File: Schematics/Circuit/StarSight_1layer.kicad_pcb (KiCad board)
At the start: 2 copper layers, 40 parts, among them IC1 LM2956-5V, J1 IR1, J10 Line1, J11 Conn_01x02, J12 Conn_01x02, J13 Conn_01x02, J14 ultSound1, J15 Conn_02x02_Counter_Clockwise, J16 ultSound1, J17 Conn_02x02_Counter_Clockwise, J18 ultSound1, J19 Conn_02x02_Counter_Clockwise, J2 Line5, J20 ultSound1, J21 Conn_01x01, J22 Conn_01x01, J23 Conn_01x01, J3 IR1, J4 Line4, J5 IR1, J6 Line3, J7 IR1, J8 Line2, J9 IR1, K1 RELAY, K2 RELAY, P1 CONN_13X2, P2 Power, Q1 Q_NMOS_GDS, Q2 Q_NMOS_GDS

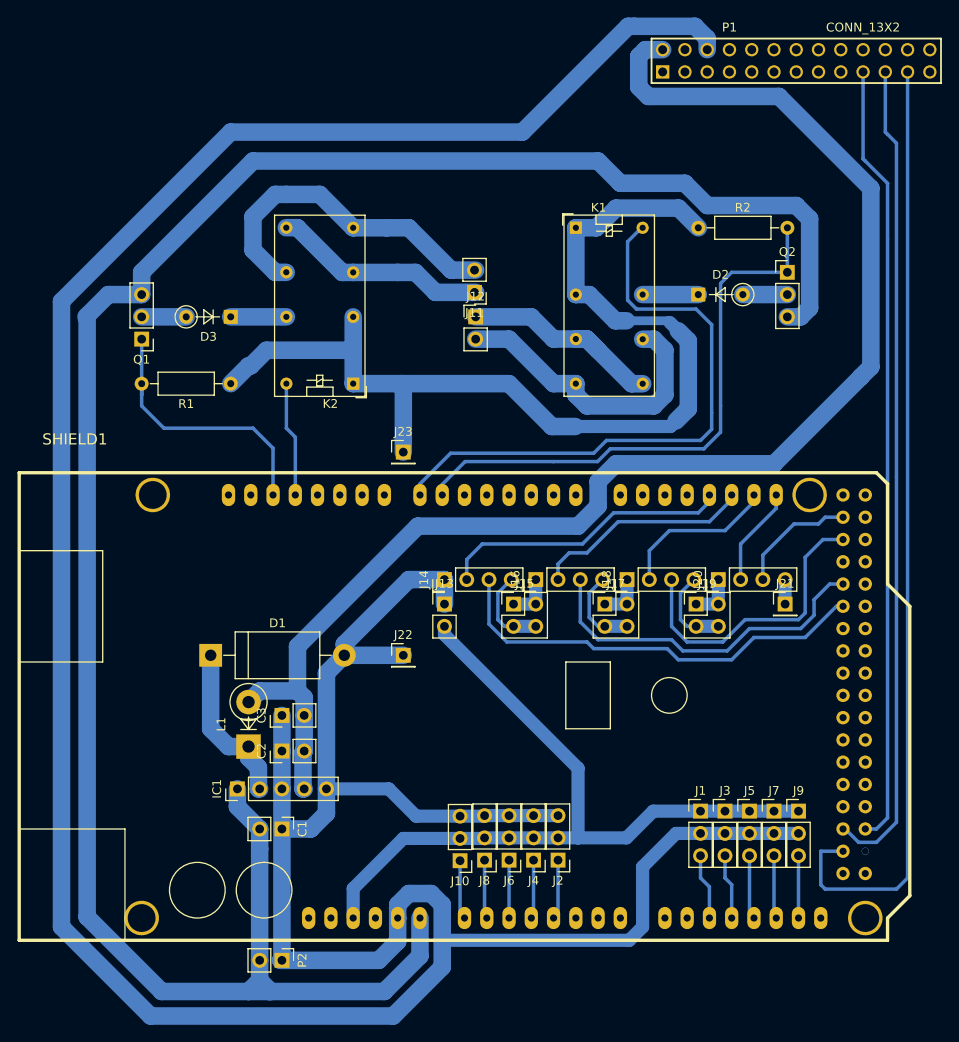
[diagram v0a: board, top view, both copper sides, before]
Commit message: Change inductor footprint
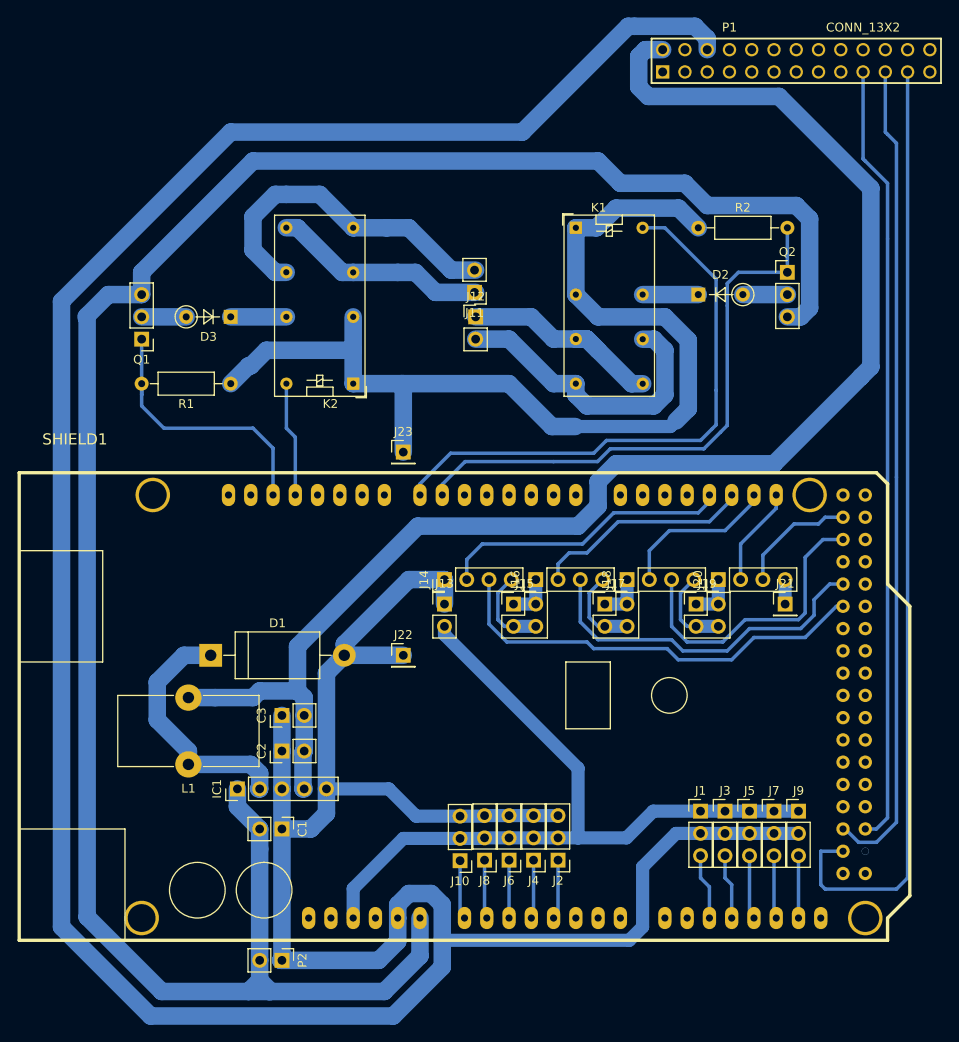
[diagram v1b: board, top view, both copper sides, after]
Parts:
- L1: footprint Diodes_THT:D_5W_P5.08mm_Vertical_KathodeUp -> Inductors_THT:L_Toroid_Vertical_L16.0mm_W8.0mm_P7.62mm
- moved L1 7.15 mm to (122.2, 98.0), turned to 180 degrees
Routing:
- net Net-(D1-Pad1): track 19.0 -> 28.7 mm
- net Net-(C2-Pad2): track 161.3 -> 168.0 mm
- net Net-(K1-Pad16): track 68.8 -> 65.4 mm

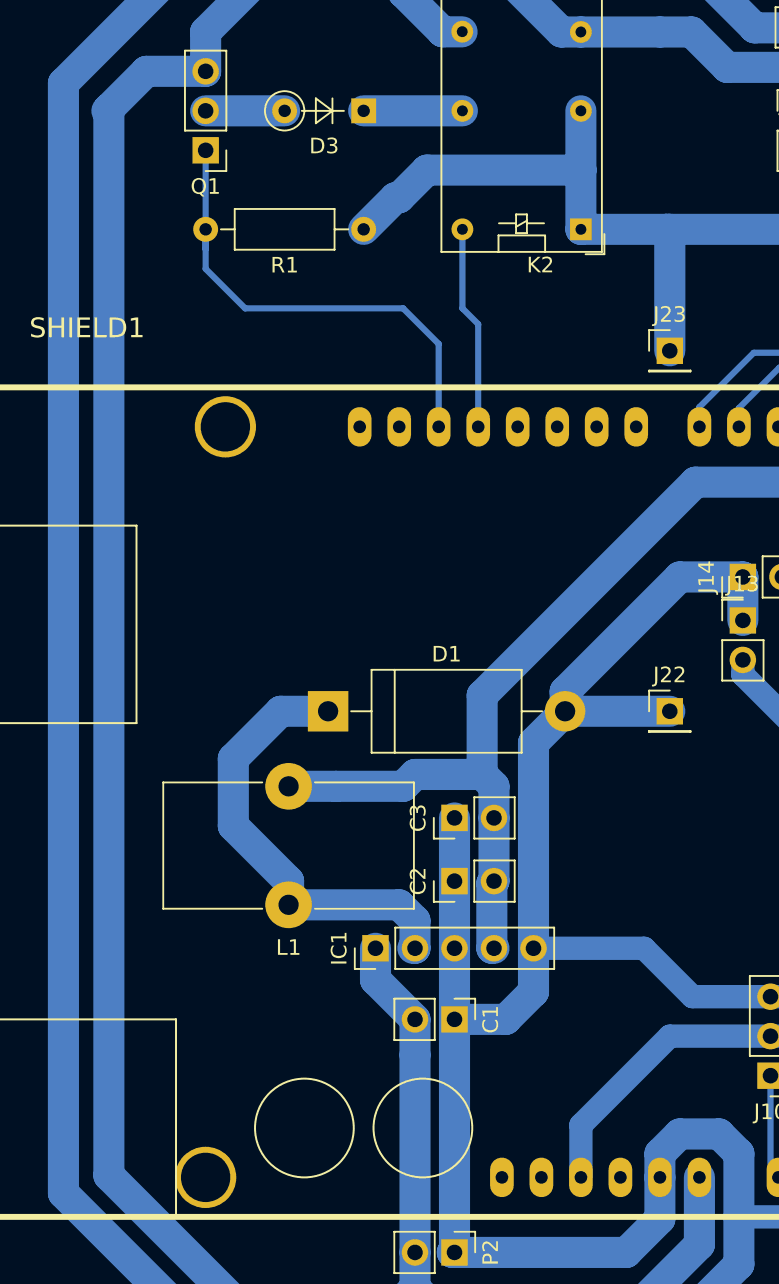
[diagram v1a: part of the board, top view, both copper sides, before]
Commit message: Add fan
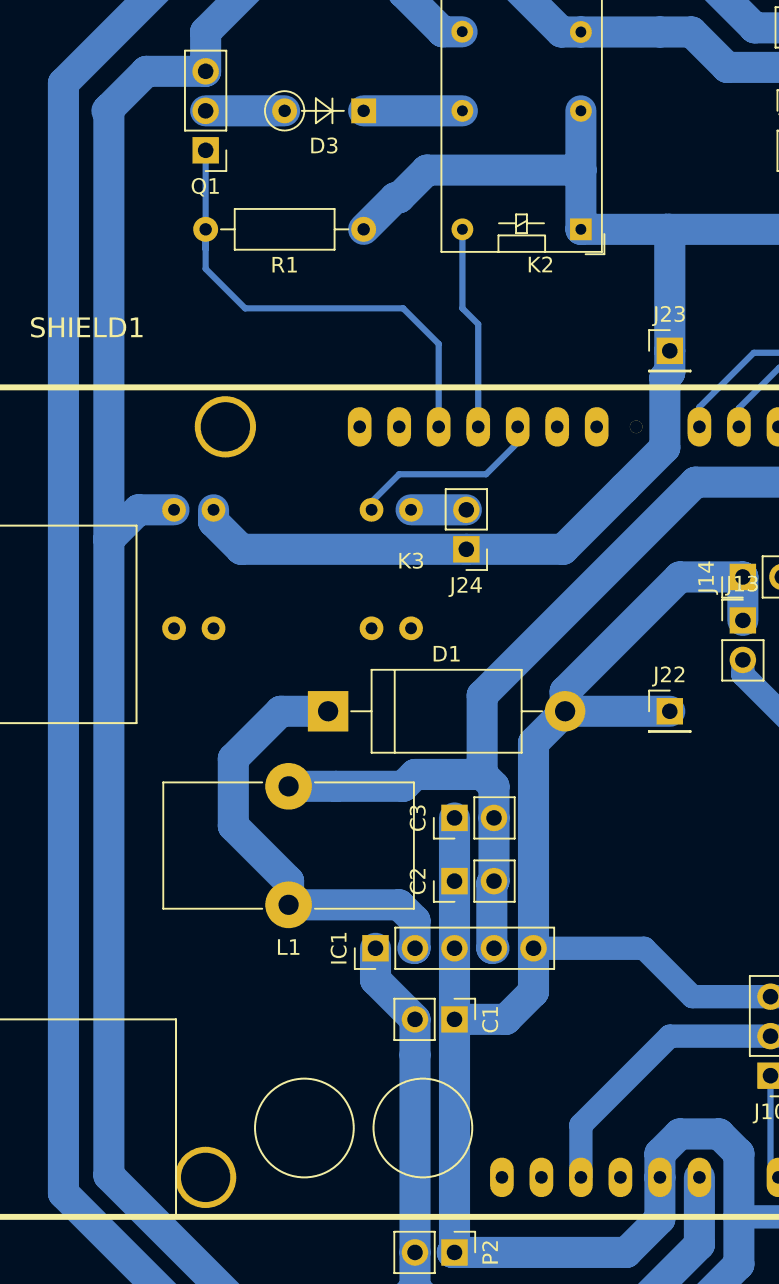
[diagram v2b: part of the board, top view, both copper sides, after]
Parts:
- added J24: Conn_01x02, Pin_Headers:Pin_Header_Straight_1x02_Pitch2.54mm, F.Cu at (133.6, 75.2)
- added K3: RELAY_s, starsight:RELAY_s, F.Cu at (130.0, 76.5)
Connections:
- K1 pad 16: Net-(K1-Pad16) -> (no net)
- K2 pad 16: Net-(K2-Pad16) -> (no net)
- SHIELD1 pad 11: (no net) -> Net-(K3-Pad2)
- SHIELD1 pad 12: Net-(K2-Pad16) -> (no net)
- SHIELD1 pad 7: Net-(K1-Pad16) -> (no net)
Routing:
- net (no net): track 0.00 -> 78.5 mm
- net Net-(K1-Pad16): track 65.4 -> 0.00 mm
- net Net-(J23-Pad1): track 118.6 -> 158.2 mm
- net Net-(K2-Pad16): track 13.1 -> 0.00 mm
- net Net-(K3-Pad2): track 0.00 -> 12.5 mm
- net +12V: track 250.1 -> 255.1 mm
- net Net-(J24-Pad2): track 0.00 -> 3.56 mm

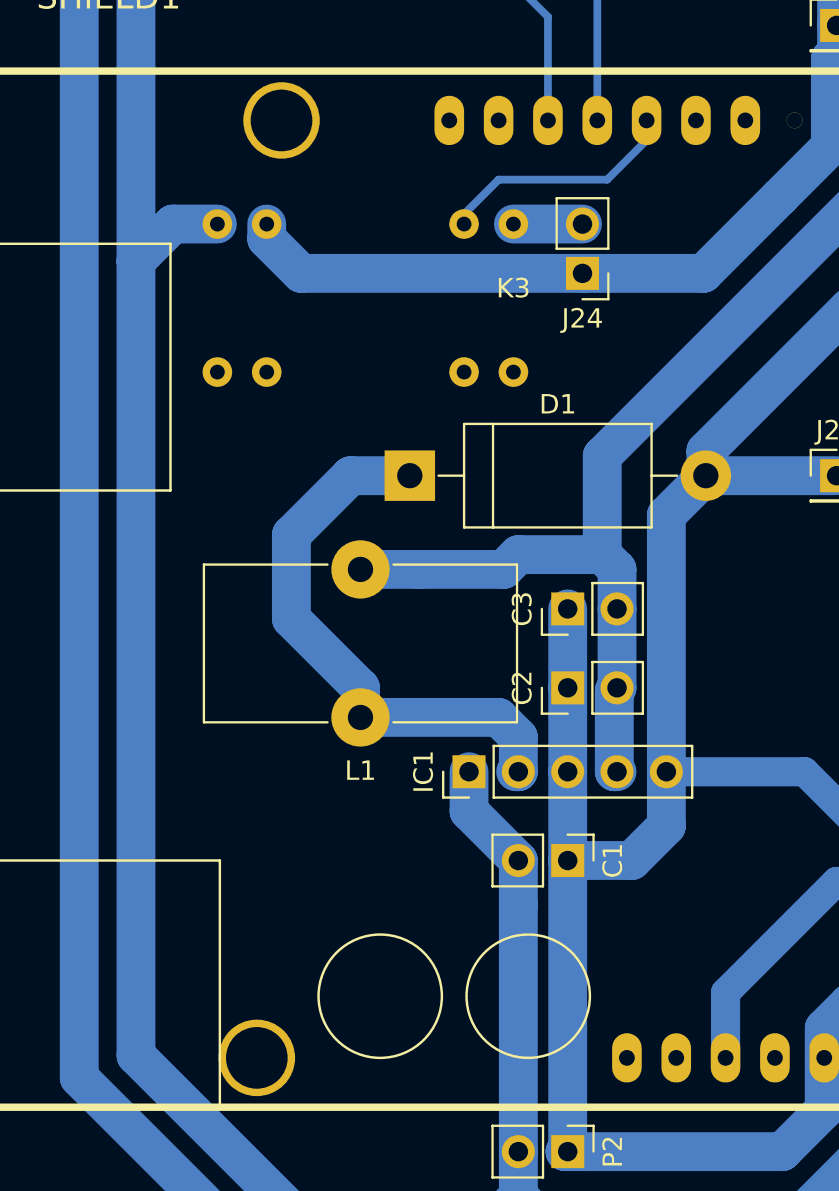
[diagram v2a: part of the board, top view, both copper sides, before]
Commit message: Edit fan relay
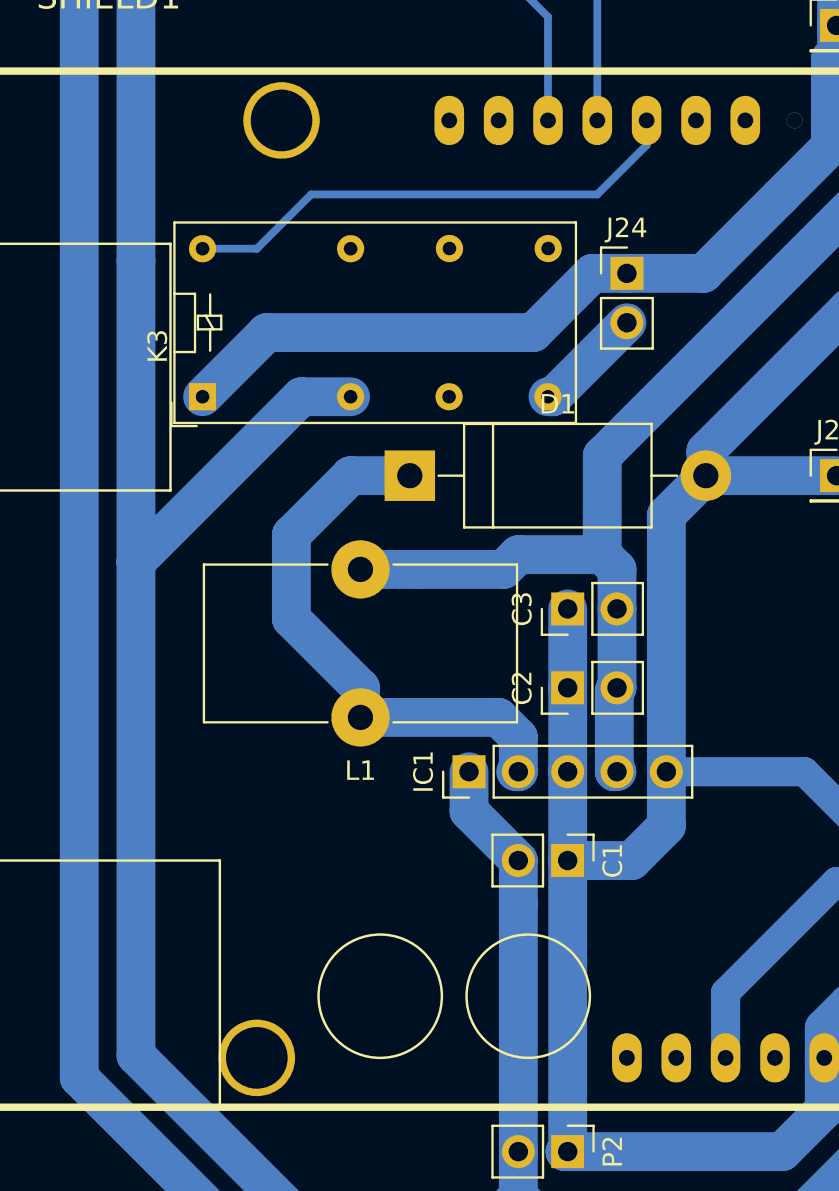
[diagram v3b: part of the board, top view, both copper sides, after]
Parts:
- K3: value RELAY_s -> RELAY; footprint starsight:RELAY_s -> Relays_THT:Relay_DPDT_Omron_G5V-2
- moved K3 16.8 mm to (114.0, 81.5), turned to 90 degrees
- moved J24 2.29 mm to (135.9, 75.2), turned to 0 degrees
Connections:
- K1 pad 16: (no net) -> Net-(K1-Pad16)
- K2 pad 16: (no net) -> Net-(K2-Pad16)
- K3 pad 1: Net-(J24-Pad2) -> Net-(J23-Pad1)
- K3 pad 8: (no net) -> Net-(J24-Pad2)
- SHIELD1 pad 11: Net-(K3-Pad2) -> Net-(K3-Pad16)
- SHIELD1 pad 12: (no net) -> Net-(K2-Pad16)
- SHIELD1 pad 7: (no net) -> Net-(K1-Pad16)
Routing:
- net (no net): track 78.5 -> 0.00 mm
- net Net-(K1-Pad16): track 0.00 -> 65.4 mm
- net Net-(K3-Pad16): track 0.00 -> 26.3 mm
- net Net-(K2-Pad16): track 0.00 -> 13.1 mm
- net Net-(K3-Pad2): track 12.5 -> 0.00 mm
- net +12V: track 255.1 -> 264.7 mm
- net Net-(J23-Pad1): track 158.2 -> 162.6 mm
- net Net-(J24-Pad2): track 3.56 -> 5.64 mm
